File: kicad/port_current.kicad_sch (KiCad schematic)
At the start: 25 parts, among them J701 USB3_A, Q701 GSF2301, Q702 2N7002, SW501 SW_Push, U701 INA381A1

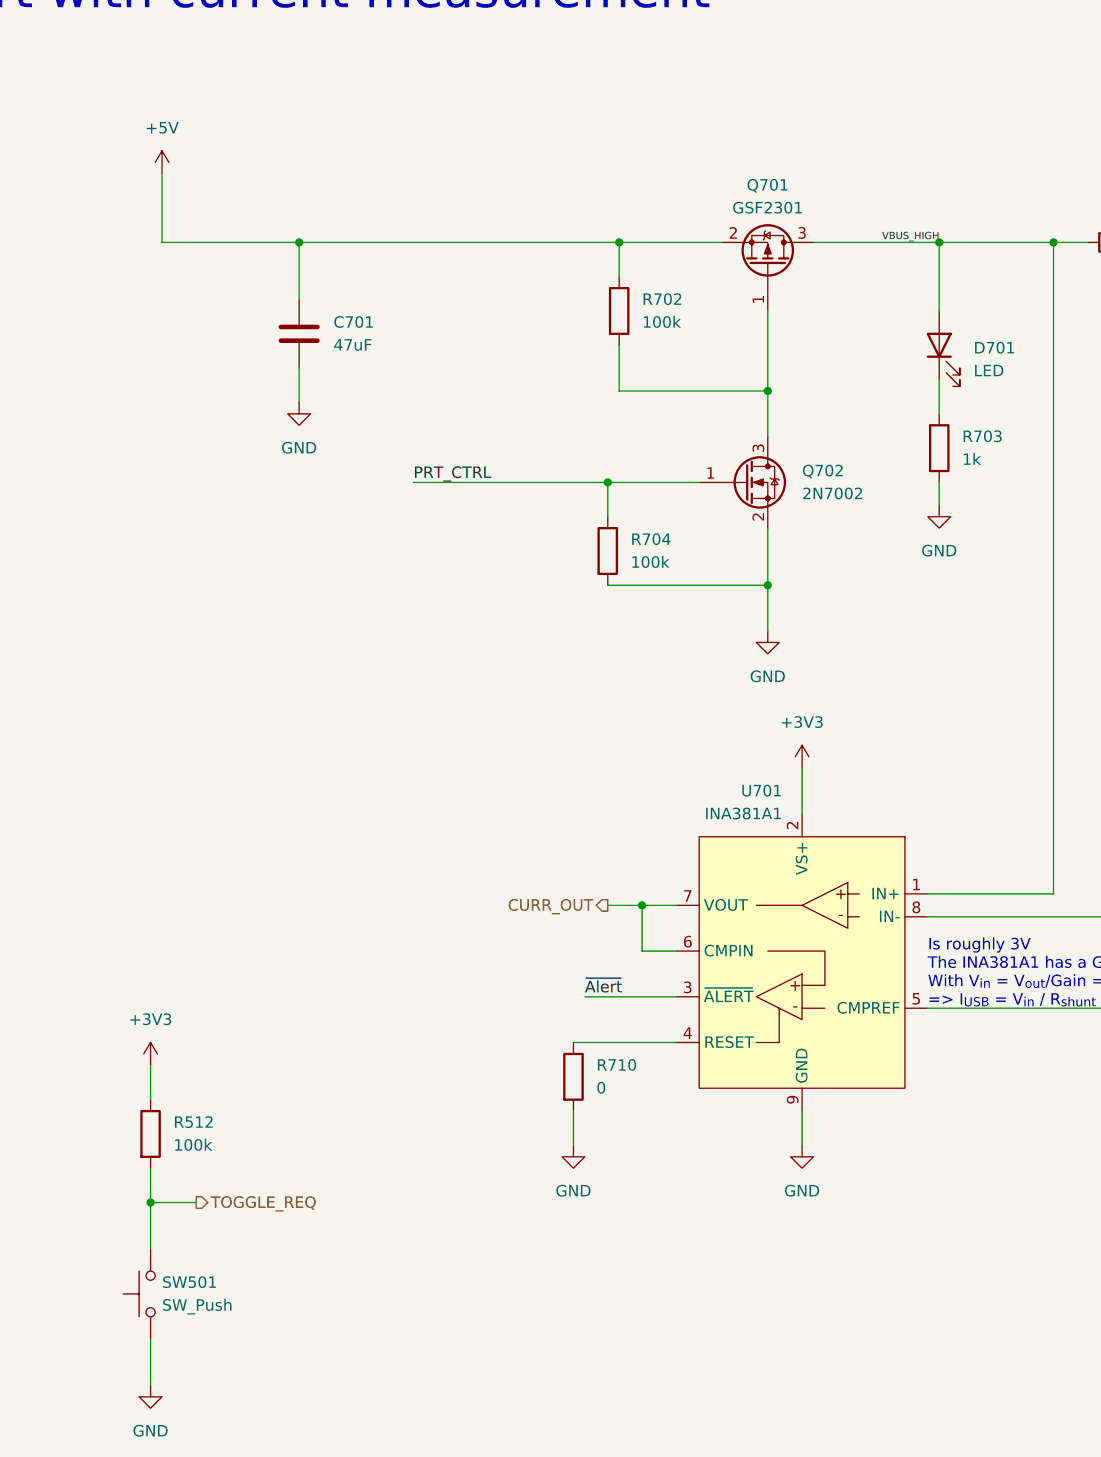
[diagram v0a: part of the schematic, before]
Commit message: First rough placement
Just to get an idea on how it might look like
Added trace widts for Differential pairs
Using 6 layers, because it makes power management easier.
Rather large PCB, but better to big, then to small.
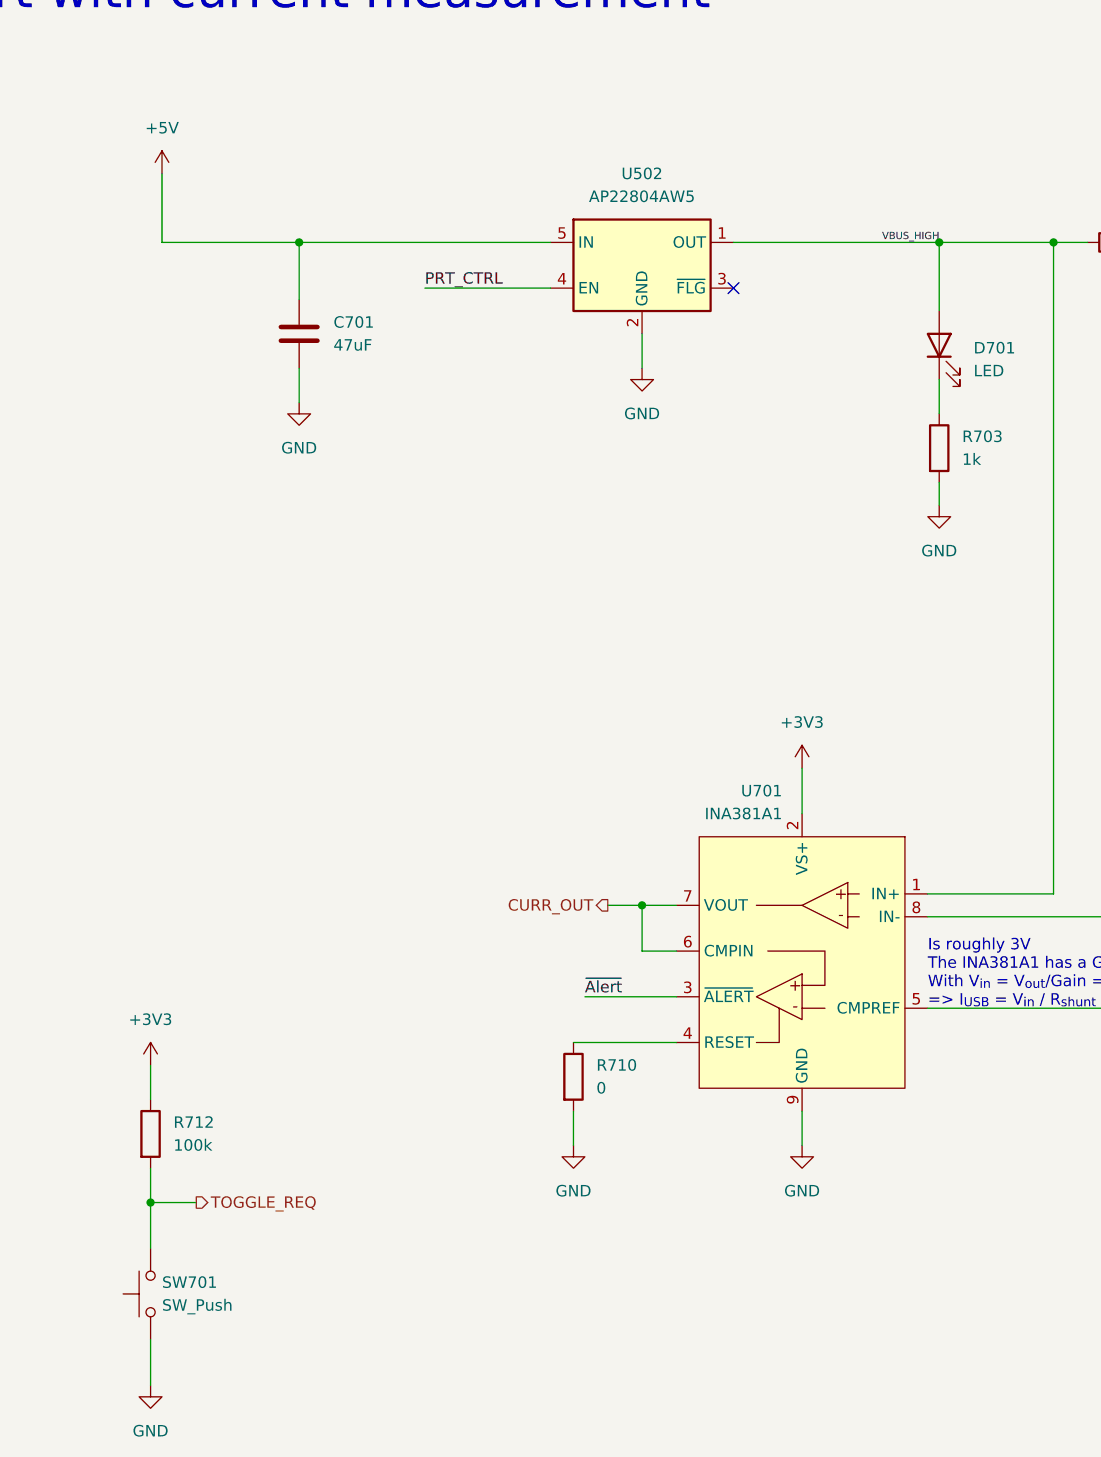
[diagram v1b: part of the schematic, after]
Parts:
- removed Q701: GSF2301, Package_TO_SOT_SMD:SOT-23, symbol Transistor_FET:AO3401A
- removed Q702: 2N7002, Package_TO_SOT_SMD:SOT-23, symbol Transistor_FET:2N7002
- removed R702, R704: 100k, Resistor_SMD:R_0603_1608Metric, symbol Device:R
- added U502: AP22804AW5, Package_TO_SOT_SMD:SOT-23-5, symbol Power_Management:AP22804AW5
- C701, C702: footprint Capacitor_SMD:C_0805_2012Metric -> Capacitor_SMD:C_1210_3225Metric
- renumbered R512 to R712, SW501 to SW701
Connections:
- net +5V: now also U502.5 (IN)
- net GND: now also U502.2 (GND)
- net PRT_CTRL: now also U502.4 (EN)
- net VBUS_HIGH: now also U502.1 (OUT)
- no-connect marks 0 -> 1

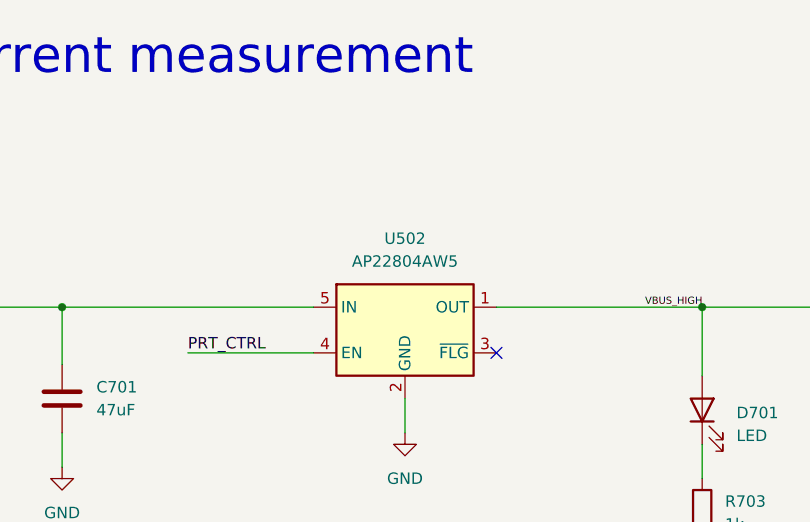
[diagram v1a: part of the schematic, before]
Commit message: Added first fanout for usb5807
Needs a lot more work, but it is a start, that allows me to concentrate
on the routing of USB signals and have the capacitors relatively close
to the hub controller.
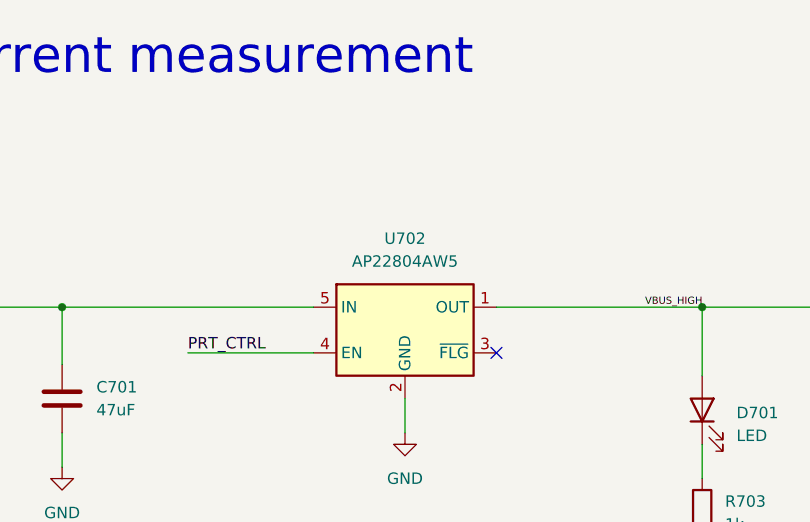
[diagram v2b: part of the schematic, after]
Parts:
- renumbered U502 to U702
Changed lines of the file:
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@@
 		(dnp no)
 		(fields_autoplaced yes)
-		(property "Reference" "U502"
+		(property "Reference" "U702"
 			(at 92.71 36.83 0)
 			(effects
@@
 		(dnp no)
 		(fields_autoplaced yes)
-		(property "Reference" "#PWR0517"
+		(property "Reference" "#PWR0717"
 			(at 92.71 64.77 0)
 			(effects

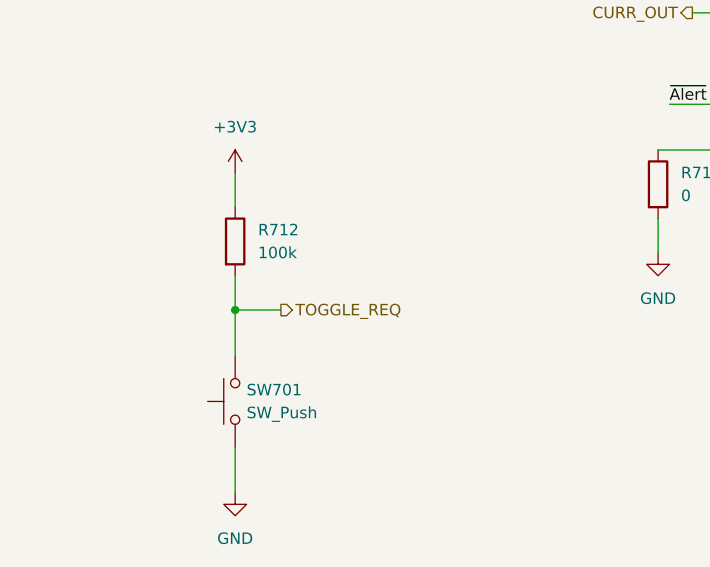
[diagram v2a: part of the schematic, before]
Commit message: Replace 1.2V LDO with switching regulator
It just feels more reliable.
Also added 0R resistors between switch and alert signal. My hope is
that I can tell the switch to diable the port by pulling the
overcurrent low.
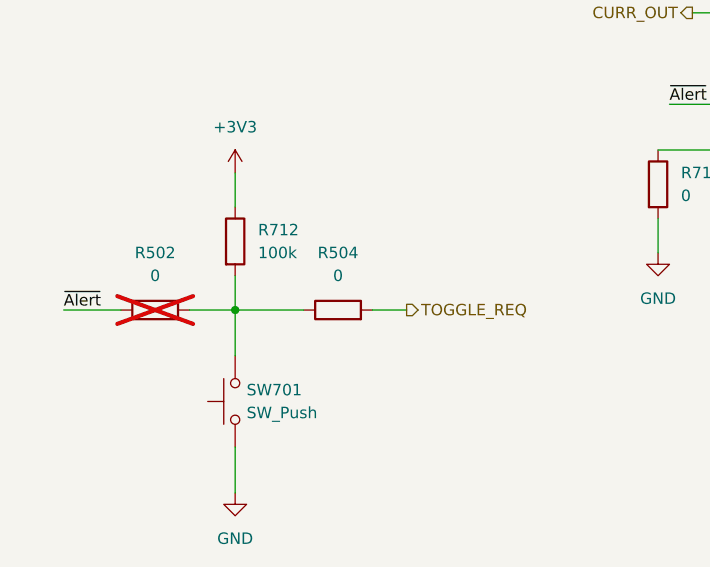
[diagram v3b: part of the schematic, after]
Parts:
- added R502, R504: 0, Resistor_SMD:R_0603_1608Metric, symbol Device:R
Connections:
- net TOGGLE_REQ: now also R504.2; no longer R712.2, SW701.2
- net ~{Alert}: now also R502.1
- new net: R502.2, R504.1, R712.2, SW701.2
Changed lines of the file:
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@@
+	(wire
+		(pts
+			(xy 38.1 156.21) (xy 38.1 151.13)
+		)
+		(stroke
+			(width 0)
+			(type default)
+		)
+	)
 	(wire
 		(pts
@@
 	(wire
 		(pts
-			(xy 38.1 151.13) (xy 43.18 151.13)
+			(xy 38.1 151.13) (xy 45.72 151.13)
 		)
 		(stroke
@@
 	(wire
 		(pts
+			(xy 33.02 151.13) (xy 38.1 151.13)
+		)
+		(stroke
+			(width 0)
+			(type default)
+		)
+	)
+	(wire
+		(pts
 			(xy 39.37 44.45) (xy 39.37 36.83)
 		)
@@
 		)
 	)
+	(wire
+		(pts
+			(xy 19.05 151.13) (xy 25.4 151.13)
+		)
+		(stroke
+			(width 0)
+			(type default)
+		)
+	)
 	(bus
 		(pts
@@
 	(wire
 		(pts
+			(xy 53.34 151.13) (xy 57.15 151.13)
+		)
+		(stroke
+			(width 0)
+			(type default)
+		)
+	)
+	(wire
+		(pts
 			(xy 252.73 72.39) (xy 252.73 74.93)
 		)
@@
 		(pts
 			(xy 96.52 123.19) (xy 92.71 123.19)
-		)
-		(stroke
-			(width 0)
-			(type default)
-		)
-	)
-	(wire
-		(pts
-			(xy 38.1 156.21) (xy 38.1 151.13)
 		)
 		(stroke
@@
 		)
 	)
-	(label "SSRX-"
-		(at 212.09 57.15 180)
+	(label "~{Alert}"
+		(at 19.05 151.13 0)
 		(fields_autoplaced yes)
 		(effects
@@
 				(size 1.27 1.27)
 			)
+			(justify left bottom)
+		)
+	)
+	(label "SSRX-"
+		(at 212.09 57.15 180)
+		(fields_autoplaced yes)
+		(effects
+			(font
+				(size 1.27 1.27)
+			)
 			(justify right bottom)
 		)
@@
 	(hierarchical_label "TOGGLE_REQ"
 		(shape output)
-		(at 43.18 151.13 0)
+		(at 57.15 151.13 0)
 		(fields_autoplaced yes)
 		(effects
@@
 			)
 			(justify right)
+		)
+	)
+	(symbol
+		(lib_id "Device:R")
+		(at 29.21 151.13 90)
+		(unit 1)
+		(exclude_from_sim no)
+		(in_bom yes)
+		(on_board yes)
+		(dnp yes)
+		(fields_autoplaced yes)
+		(property "Reference" "R502"
+			(at 29.21 144.78 90)
+			(effects
+				(font
+					(size 1.27 1.27)
+				)
+			)
+		)
+		(property "Value" "0"
+			(at 29.21 147.32 90)
+			(effects
+				(font
+					(size 1.27 1.27)
+				)
+			)
+		)
+		(property "Footprint" "Resistor_SMD:R_0603_1608Metric"
+			(at 29.21 152.908 90)
+			(effects
+				(font
+					(size 1.27 1.27)
+				)
+				(hide yes)
+			)
+		)
+		(property "Datasheet" "~"
+			(at 29.21 151.13 0)
+			(effects
+				(font
+					(size 1.27 1.27)
+				)
+				(hide yes)
+			)
+		)
+		(property "Description" "Resistor"
+			(at 29.21 151.13 0)
+			(effects
+				(font
+					(size 1.27 1.27)
+				)
+				(hide yes)
+			)
+		)
+		(pin "1"
+		)
+		(pin "2"
+		)
+		(instances
+			(project "usb3-hub"
+				(path "/fa2d0b8b-d66f-4d1f-bda6-9ad6b6242db5/a4bd64a1-b253-4895-8aa2-8555fbc6d895"
+					(reference "R702")
+					(unit 1)
+				)
+				(path "/fa2d0b8b-d66f-4d1f-bda6-9ad6b6242db5/ba351116-7014-4061-a218-c14d18cd07d7"
+					(reference "R502")
+					(unit 1)
+				)
+				(path "/fa2d0b8b-d66f-4d1f-bda6-9ad6b6242db5/e8738ec1-5cf3-402b-90e5-f9a9a49acb36"
+					(reference "R602")
+					(unit 1)
+				)
+			)
 		)
 	)
@@
 					(unit 1)
 				)
+			)
+		)
+	)
+	(symbol
+		(lib_id "Device:R")
+		(at 49.53 151.13 90)
+		(unit 1)
+		(exclude_from_sim no)
+		(in_bom yes)
+		(on_board yes)
+		(dnp no)
+		(fields_autoplaced yes)
+		(property "Reference" "R504"
+			(at 49.53 144.78 90)
+			(effects
+				(font
+					(size 1.27 1.27)
+				)
+			)
+		)
+		(property "Value" "0"
+			(at 49.53 147.32 90)
+			(effects
+				(font
+					(size 1.27 1.27)
+				)
+			)
+		)
+		(property "Footprint" "Resistor_SMD:R_0603_1608Metric"
+			(at 49.53 152.908 90)
+			(effects
+				(font
+					(size 1.27 1.27)
+				)
+				(hide yes)
+			)
+		)
+		(property "Datasheet" "~"
+			(at 49.53 151.13 0)
+			(effects
+				(font
+					(size 1.27 1.27)
+				)
+				(hide yes)
+			)
+		)
+		(property "Description" "Resistor"
+			(at 49.53 151.13 0)
+			(effects
+				(font
+					(size 1.27 1.27)
+				)
+				(hide yes)
+			)
+		)
+		(pin "1"
+		)
+		(pin "2"
+		)
+		(instances
+			(project "usb3-hub"
+				(path "/fa2d0b8b-d66f-4d1f-bda6-9ad6b6242db5/a4bd64a1-b253-4895-8aa2-8555fbc6d895"
+					(reference "R704")
+					(unit 1)
+				)
+				(path "/fa2d0b8b-d66f-4d1f-bda6-9ad6b6242db5/ba351116-7014-4061-a218-c14d18cd07d7"
+					(reference "R504")
+					(unit 1)
+				)
+				(path "/fa2d0b8b-d66f-4d1f-bda6-9ad6b6242db5/e8738ec1-5cf3-402b-90e5-f9a9a49acb36"
+					(reference "R604")
+					(unit 1)
+				)

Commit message: Some more routing
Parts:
- D701: value LED -> GREEN
- D702: value LED -> RED
- D703: value LED -> BLUE
- renumbered R502 to R702, R504 to R704
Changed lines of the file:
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@@
 	)
 	(junction
-		(at 152.4 44.45)
-		(diameter 0)
-		(color 0 0 0 0)
-	)
-	(junction
 		(at 179.07 129.54)
 		(diameter 0)
@@
 	)
 	(junction
+		(at 153.67 44.45)
+		(diameter 0)
+		(color 0 0 0 0)
+	)
+	(junction
 		(at 229.87 44.45)
 		(diameter 0)
@@
 	(wire
 		(pts
-			(xy 152.4 44.45) (xy 152.4 119.38)
-		)
-		(stroke
-			(width 0)
-			(type default)
-		)
-	)
-	(wire
-		(pts
 			(xy 252.73 74.93) (xy 264.16 74.93)
 		)
@@
 	(wire
 		(pts
-			(xy 152.4 44.45) (xy 165.1 44.45)
-		)
-		(stroke
-			(width 0)
-			(type default)
-		)
-	)
-	(wire
-		(pts
 			(xy 165.1 58.42) (xy 165.1 62.23)
 		)
@@
 	(wire
 		(pts
-			(xy 125.73 44.45) (xy 138.43 44.45)
+			(xy 138.43 44.45) (xy 138.43 116.84)
 		)
 		(stroke
@@
 	(wire
 		(pts
-			(xy 261.62 137.16) (xy 267.97 137.16)
+			(xy 125.73 44.45) (xy 138.43 44.45)
 		)
 		(stroke
@@
 	(wire
 		(pts
-			(xy 152.4 44.45) (xy 149.86 44.45)
+			(xy 261.62 137.16) (xy 267.97 137.16)
 		)
 		(stroke
@@
 	(wire
 		(pts
-			(xy 165.1 44.45) (xy 229.87 44.45)
+			(xy 149.86 44.45) (xy 153.67 44.45)
 		)
 		(stroke
@@
 		)
 	)
-	(bus
+	(wire
 		(pts
-			(xy 196.85 59.69) (xy 196.85 62.23)
+			(xy 165.1 44.45) (xy 229.87 44.45)
 		)
 		(stroke
@@
 		)
 	)
-	(wire
+	(bus
 		(pts
-			(xy 138.43 116.84) (xy 138.43 44.45)
+			(xy 196.85 59.69) (xy 196.85 62.23)
 		)
 		(stroke
@@
 		)
 	)
+	(wire
+		(pts
+			(xy 153.67 44.45) (xy 153.67 119.38)
+		)
+		(stroke
+			(width 0)
+			(type default)
+		)
+	)
 	(bus
 		(pts
@@
 	(wire
 		(pts
+			(xy 153.67 44.45) (xy 165.1 44.45)
+		)
+		(stroke
+			(width 0)
+			(type default)
+		)
+	)
+	(wire
+		(pts
 			(xy 252.73 74.93) (xy 252.73 77.47)
 		)
@@
 	(wire
 		(pts
-			(xy 124.46 119.38) (xy 152.4 119.38)
+			(xy 124.46 119.38) (xy 153.67 119.38)
 		)
 		(stroke
@@
 		(dnp yes)
 		(fields_autoplaced yes)
-		(property "Reference" "R502"
+		(property "Reference" "R702"
 			(at 29.21 144.78 90)
 			(effects
@@
 			)
 		)
-		(property "Value" "LED"
+		(property "Value" "BLUE"
 			(at 271.78 147.6374 90)
 			(effects
@@
 			)
 		)
-		(property "Datasheet" ""
+		(property "Datasheet" "https://www.ti.com/lit/ds/symlink/ina381.pdf"
 			(at 111.76 116.84 0)
 			(effects
@@
 		(dnp no)
 		(fields_autoplaced yes)
-		(property "Reference" "R504"
+		(property "Reference" "R704"
 			(at 49.53 144.78 90)
 			(effects
@@
 			)
 		)
-		(property "Value" "LED"
+		(property "Value" "RED"
 			(at 271.78 132.3974 90)
 			(effects
@@
 			)
 		)
-		(property "Value" "LED"
+		(property "Value" "GREEN"
 			(at 129.54 58.7374 90)
 			(effects
